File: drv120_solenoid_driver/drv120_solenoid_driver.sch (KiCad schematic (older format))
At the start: 8 parts, among them J1 Power, J2 Enable, J3 Solenoid, U1 drv120

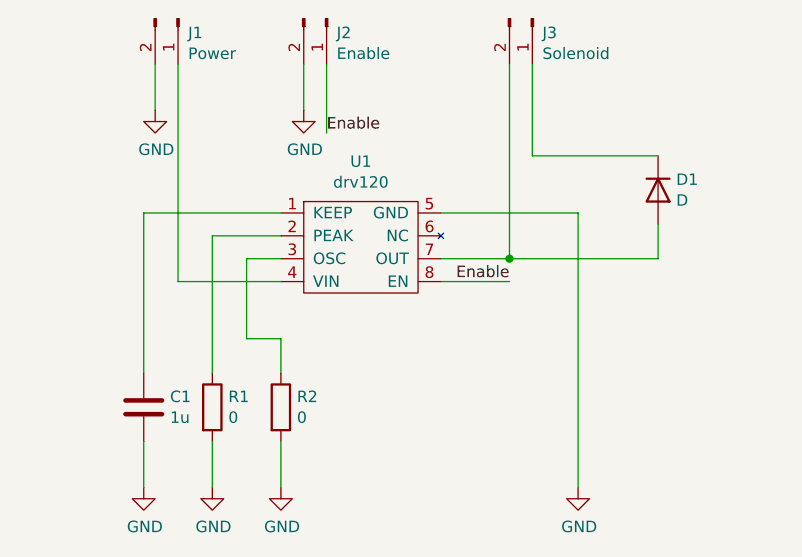
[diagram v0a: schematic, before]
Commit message: Single sided PCB
First pass at a single sided PCB
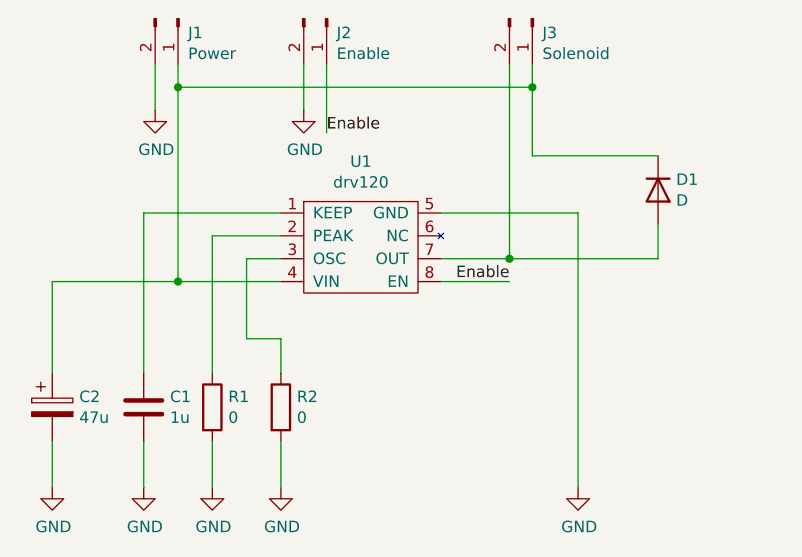
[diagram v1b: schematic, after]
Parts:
- added C2: 47u, Capacitor_SMD:CP_Elec_6.3x5.8, symbol Device:CP
- C1: footprint (none) -> Capacitor_SMD:C_0805_2012Metric_Pad1.15x1.40mm_HandSolder
- D1: footprint (none) -> Diode_SMD:D_SMA_Handsoldering
- J1, J2, J3: footprint (none) -> Connector_PinHeader_2.54mm:PinHeader_1x02_P2.54mm_Vertical
- R1, R2: footprint (none) -> Resistor_SMD:R_0805_2012Metric
- U1: footprint (none) -> Package_SO:Texas_R-PDSO-G8_EP2.95x4.9mm_Mask2.4x3.1mm
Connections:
- net GND: now also C2.2
- net at J1.1 (Pin_1), U1.4 (VIN): now also D1.1 (K), J3.1 (Pin_1), C2.1
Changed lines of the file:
@@
 EESchema Schematic File Version 4
+LIBS:drv120_solenoid_driver-cache
 EELAYER 30 0
 EELAYER END
@@
 F 0 "U1" H 5750 3175 50  0000 C CNN
 F 1 "drv120" H 5750 3084 50  0000 C CNN
-F 2 "" H 5700 3000 50  0001 C CNN
+F 2 "Package_SO:Texas_R-PDSO-G8_EP2.95x4.9mm_Mask2.4x3.1mm" H 5700 3000 50  0001 C CNN
 F 3 "" H 5700 3000 50  0001 C CNN
 	1    5500 3000
@@
 F 0 "D1" V 7004 3029 50  0000 L CNN
 F 1 "D" V 7095 3029 50  0000 L CNN
-F 2 "" H 7050 2950 50  0001 C CNN
+F 2 "Diode_SMD:D_SMA_Handsoldering" H 7050 2950 50  0001 C CNN
 F 3 "~" H 7050 2950 50  0001 C CNN
 	1    7050 2950
@@
 F 0 "C1" H 4915 3946 50  0000 L CNN
 F 1 "1u" H 4915 3855 50  0000 L CNN
-F 2 "" H 4838 3750 50  0001 C CNN
+F 2 "Capacitor_SMD:C_0805_2012Metric_Pad1.15x1.40mm_HandSolder" H 4838 3750 50  0001 C CNN
 F 3 "~" H 4800 3900 50  0001 C CNN
 	1    4800 3900
@@
 F 0 "R1" H 5170 3946 50  0000 L CNN
 F 1 "0" H 5170 3855 50  0000 L CNN
-F 2 "" V 5030 3900 50  0001 C CNN
+F 2 "Resistor_SMD:R_0805_2012Metric" V 5030 3900 50  0001 C CNN
 F 3 "~" H 5100 3900 50  0001 C CNN
 	1    5100 3900
@@
 F 0 "R2" H 5470 3946 50  0000 L CNN
 F 1 "0" H 5470 3855 50  0000 L CNN
-F 2 "" V 5330 3900 50  0001 C CNN
+F 2 "Resistor_SMD:R_0805_2012Metric" V 5330 3900 50  0001 C CNN
 F 3 "~" H 5400 3900 50  0001 C CNN
 	1    5400 3900
@@
 F 0 "J3" V 6562 2244 50  0000 L CNN
 F 1 "Solenoid" V 6653 2244 50  0000 L CNN
-F 2 "" H 6500 2200 50  0001 C CNN
+F 2 "Connector_PinHeader_2.54mm:PinHeader_1x02_P2.54mm_Vertical" H 6500 2200 50  0001 C CNN
 F 3 "~" H 6500 2200 50  0001 C CNN
 	1    6500 2200
@@
 F 0 "J1" V 5012 2244 50  0000 L CNN
 F 1 "Power" V 5103 2244 50  0000 L CNN
-F 2 "" H 4950 2200 50  0001 C CNN
+F 2 "Connector_PinHeader_2.54mm:PinHeader_1x02_P2.54mm_Vertical" H 4950 2200 50  0001 C CNN
 F 3 "~" H 4950 2200 50  0001 C CNN
 	1    4950 2200
@@
 F 0 "J2" V 5662 2244 50  0000 L CNN
 F 1 "Enable" V 5753 2244 50  0000 L CNN
-F 2 "" H 5600 2200 50  0001 C CNN
+F 2 "Connector_PinHeader_2.54mm:PinHeader_1x02_P2.54mm_Vertical" H 5600 2200 50  0001 C CNN
 F 3 "~" H 5600 2200 50  0001 C CNN
 	1    5600 2200
@@
 $EndComp
 $Comp
-L power:GND #PWR?
+L power:GND #PWR0101
 U 1 1 5E5535B5
 P 5400 4250
-F 0 "#PWR?" H 5400 4000 50  0001 C CNN
+F 0 "#PWR0101" H 5400 4000 50  0001 C CNN
 F 1 "GND" H 5405 4077 50  0000 C CNN
 F 2 "" H 5400 4250 50  0001 C CNN
@@
 $EndComp
 $Comp
-L power:GND #PWR?
+L power:GND #PWR0102
 U 1 1 5E5538A5
 P 5100 4250
-F 0 "#PWR?" H 5100 4000 50  0001 C CNN
+F 0 "#PWR0102" H 5100 4000 50  0001 C CNN
 F 1 "GND" H 5105 4077 50  0000 C CNN
 F 2 "" H 5100 4250 50  0001 C CNN
@@
 $EndComp
 $Comp
-L power:GND #PWR?
+L power:GND #PWR0103
 U 1 1 5E5539D8
 P 4800 4250
-F 0 "#PWR?" H 4800 4000 50  0001 C CNN
+F 0 "#PWR0103" H 4800 4000 50  0001 C CNN
 F 1 "GND" H 4805 4077 50  0000 C CNN
 F 2 "" H 4800 4250 50  0001 C CNN
@@
 $EndComp
 $Comp
-L power:GND #PWR?
+L power:GND #PWR0104
 U 1 1 5E553BFA
 P 6700 4250
-F 0 "#PWR?" H 6700 4000 50  0001 C CNN
+F 0 "#PWR0104" H 6700 4000 50  0001 C CNN
 F 1 "GND" H 6705 4077 50  0000 C CNN
 F 2 "" H 6700 4250 50  0001 C CNN
@@
 	5400 3350 4950 3350
 Wire Wire Line
-	4950 3350 4950 2400
-$Comp
-L power:GND #PWR?
+	4950 3350 4950 2500
+$Comp
+L power:GND #PWR0105
 U 1 1 5E555804
 P 4850 2600
-F 0 "#PWR?" H 4850 2350 50  0001 C CNN
+F 0 "#PWR0105" H 4850 2350 50  0001 C CNN
 F 1 "GND" H 4855 2427 50  0000 C CNN
 F 2 "" H 4850 2600 50  0001 C CNN
@@
 	4850 2400 4850 2600
 $Comp
-L power:GND #PWR?
+L power:GND #PWR0106
 U 1 1 5E5560E2
 P 5500 2600
-F 0 "#PWR?" H 5500 2350 50  0001 C CNN
+F 0 "#PWR0106" H 5500 2350 50  0001 C CNN
 F 1 "GND" H 5505 2427 50  0000 C CNN
 F 2 "" H 5500 2600 50  0001 C CNN
@@
 	7050 2800 6500 2800
 Wire Wire Line
-	6500 2800 6500 2400
+	6500 2800 6500 2500
 Wire Wire Line
 	6400 2400 6400 3250
@@
 Wire Wire Line
 	6700 3050 6700 4250
+Wire Wire Line
+	4950 2500 6500 2500
+Connection ~ 4950 2500
+Wire Wire Line
+	4950 2500 4950 2400
+Connection ~ 6500 2500
+Wire Wire Line
+	6500 2500 6500 2400
+$Comp
+L Device:CP C2
+U 1 1 5E55F875
+P 4400 3900
+F 0 "C2" H 4518 3946 50  0000 L CNN
+F 1 "47u" H 4518 3855 50  0000 L CNN
+F 2 "Capacitor_SMD:CP_Elec_6.3x5.8" H 4438 3750 50  0001 C CNN
+F 3 "~" H 4400 3900 50  0001 C CNN
+	1    4400 3900
+	1    0    0    -1
+$EndComp
+$Comp
+L power:GND #PWR01
+U 1 1 5E55FF5C
+P 4400 4250
+F 0 "#PWR01" H 4400 4000 50  0001 C CNN
+F 1 "GND" H 4405 4077 50  0000 C CNN
+F 2 "" H 4400 4250 50  0001 C CNN
+F 3 "" H 4400 4250 50  0001 C CNN
+	1    4400 4250
+	1    0    0    -1
+$EndComp
+Connection ~ 4950 3350
+Wire Wire Line
+	4400 3350 4400 3750
+Wire Wire Line
+	4400 3350 4950 3350
+Wire Wire Line
+	4400 4050 4400 4250
 $EndSCHEMATC

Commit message: Changed to JST-PH 2.00 TH connectors
Also changed input connector to a single 3 pin JST. Solenoid is on a 2 pin JST.
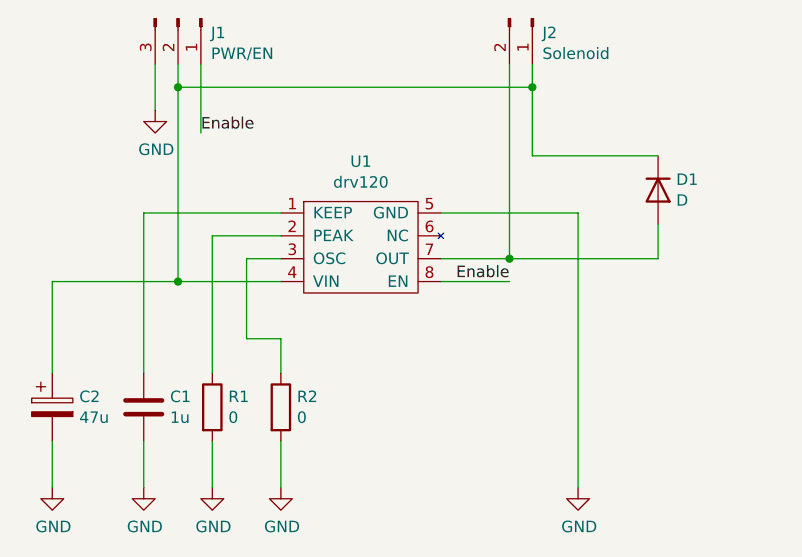
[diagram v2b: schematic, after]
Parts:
- removed J1: Power, Connector_PinHeader_2.54mm:PinHeader_1x02_P2.54mm_Vertical, symbol Connector:Conn_01x02_Male
- removed J2: Enable, Connector_PinHeader_2.54mm:PinHeader_1x02_P2.54mm_Vertical, symbol Connector:Conn_01x02_Male
- added J1: PWR/EN, Connector_JST:JST_PH_B3B-PH-K_1x03_P2.00mm_Vertical, symbol Connector:Conn_01x03_Male
- J2: renamed from J3; footprint Connector_PinHeader_2.54mm:PinHeader_1x02_P2.54mm_Vertical -> Connector_JST:JST_PH_B2B-PH-K_1x02_P2.00mm_Vertical
- U1: footprint Package_SO:Texas_R-PDSO-G8_EP2.95x4.9mm_Mask2.4x3.1mm -> Package_SO:TSSOP-8_4.4x3mm_P0.65mm
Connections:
- net Enable: now also J1.1 (Pin_1)
- net GND: now also J1.3 (Pin_3)
- net at C2.1, D1.1 (K), J2.1 (Pin_1)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: now also J1.2 (Pin_2)
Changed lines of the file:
@@
 EESchema Schematic File Version 4
-LIBS:drv120_solenoid_driver-cache
 EELAYER 30 0
 EELAYER END
@@
 F 0 "U1" H 5750 3175 50  0000 C CNN
 F 1 "drv120" H 5750 3084 50  0000 C CNN
-F 2 "Package_SO:Texas_R-PDSO-G8_EP2.95x4.9mm_Mask2.4x3.1mm" H 5700 3000 50  0001 C CNN
+F 2 "Package_SO:TSSOP-8_4.4x3mm_P0.65mm" H 5700 3000 50  0001 C CNN
 F 3 "" H 5700 3000 50  0001 C CNN
 	1    5500 3000
@@
 $EndComp
 $Comp
-L Connector:Conn_01x02_Male J3
+L Connector:Conn_01x02_Male J2
 U 1 1 5E549C14
 P 6500 2200
-F 0 "J3" V 6562 2244 50  0000 L CNN
+F 0 "J2" V 6562 2244 50  0000 L CNN
 F 1 "Solenoid" V 6653 2244 50  0000 L CNN
-F 2 "Connector_PinHeader_2.54mm:PinHeader_1x02_P2.54mm_Vertical" H 6500 2200 50  0001 C CNN
+F 2 "Connector_JST:JST_PH_B2B-PH-K_1x02_P2.00mm_Vertical" H 6500 2200 50  0001 C CNN
 F 3 "~" H 6500 2200 50  0001 C CNN
 	1    6500 2200
@@
 Wire Wire Line
 	5250 3250 5250 3600
-$Comp
-L Connector:Conn_01x02_Male J1
-U 1 1 5E551684
-P 4950 2200
-F 0 "J1" V 5012 2244 50  0000 L CNN
-F 1 "Power" V 5103 2244 50  0000 L CNN
-F 2 "Connector_PinHeader_2.54mm:PinHeader_1x02_P2.54mm_Vertical" H 4950 2200 50  0001 C CNN
-F 3 "~" H 4950 2200 50  0001 C CNN
-	1    4950 2200
-	0    1    1    0
-$EndComp
-$Comp
-L Connector:Conn_01x02_Male J2
-U 1 1 5E5522D2
-P 5600 2200
-F 0 "J2" V 5662 2244 50  0000 L CNN
-F 1 "Enable" V 5753 2244 50  0000 L CNN
-F 2 "Connector_PinHeader_2.54mm:PinHeader_1x02_P2.54mm_Vertical" H 5600 2200 50  0001 C CNN
-F 3 "~" H 5600 2200 50  0001 C CNN
-	1    5600 2200
-	0    1    1    0
-$EndComp
 $Comp
 L power:GND #PWR0101
@@
 Wire Wire Line
 	4850 2400 4850 2600
-$Comp
-L power:GND #PWR0106
-U 1 1 5E5560E2
-P 5500 2600
-F 0 "#PWR0106" H 5500 2350 50  0001 C CNN
-F 1 "GND" H 5505 2427 50  0000 C CNN
-F 2 "" H 5500 2600 50  0001 C CNN
-F 3 "" H 5500 2600 50  0001 C CNN
-	1    5500 2600
-	1    0    0    -1
-$EndComp
-Wire Wire Line
-	5500 2600 5500 2400
-Wire Wire Line
-	5600 2400 5600 2700
-Text Label 5600 2700 0    50   ~ 0
+Wire Wire Line
+	5050 2400 5050 2700
+Text Label 5050 2700 0    50   ~ 0
 Enable
 Wire Wire Line
@@
 Wire Wire Line
 	4400 4050 4400 4250
+$Comp
+L Connector:Conn_01x03_Male J1
+U 1 1 6178519F
+P 4950 2200
+F 0 "J1" V 5012 2344 50  0000 L CNN
+F 1 "PWR/EN" V 5103 2344 50  0000 L CNN
+F 2 "Connector_JST:JST_PH_B3B-PH-K_1x03_P2.00mm_Vertical" H 4950 2200 50  0001 C CNN
+F 3 "~" H 4950 2200 50  0001 C CNN
+	1    4950 2200
+	0    1    1    0
+$EndComp
 $EndSCHEMATC

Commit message: Add component part numbers
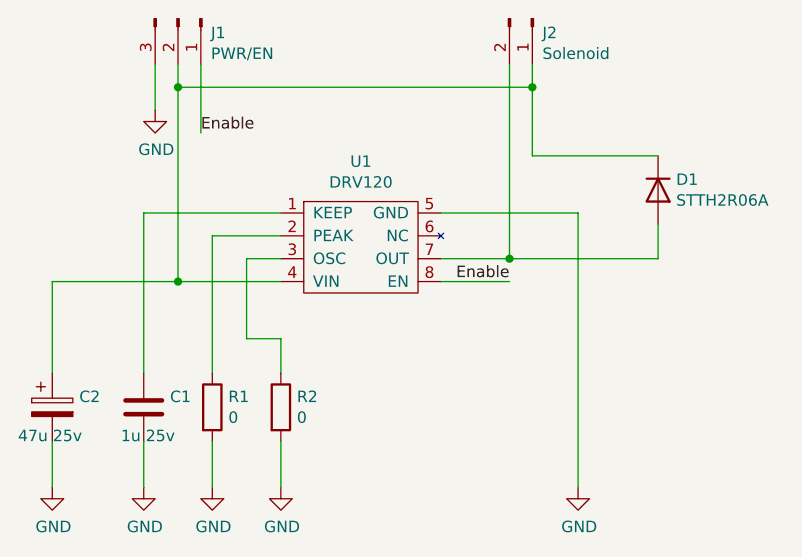
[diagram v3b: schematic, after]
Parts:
- C1: value 1u -> 1u 25v; LCSC (none) -> C146681
- C2: value 47u -> 47u 25v; LCSC (none) -> C336364
- D1: value D -> STTH2R06A; LCSC (none) -> Alt part no: C908656; Part No (none) -> STTH2R06A
- J1: LCSC (none) -> C146083
- J2: LCSC (none) -> C8886
- R1, R2: LCSC (none) -> C103901
- U1: value drv120 -> DRV120
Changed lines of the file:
@@
 $EndDescr
-$Comp
-L custom:drv120 U1
-U 1 1 5E545EF0
-P 5500 3000
-F 0 "U1" H 5750 3175 50  0000 C CNN
-F 1 "drv120" H 5750 3084 50  0000 C CNN
-F 2 "Package_SO:TSSOP-8_4.4x3mm_P0.65mm" H 5700 3000 50  0001 C CNN
-F 3 "" H 5700 3000 50  0001 C CNN
-	1    5500 3000
-	1    0    0    -1
-$EndComp
 $Comp
 L Device:D D1
@@
 P 7050 2950
 F 0 "D1" V 7004 3029 50  0000 L CNN
-F 1 "D" V 7095 3029 50  0000 L CNN
+F 1 "STTH2R06A" V 7095 3029 50  0000 L CNN
 F 2 "Diode_SMD:D_SMA_Handsoldering" H 7050 2950 50  0001 C CNN
-F 3 "~" H 7050 2950 50  0001 C CNN
+F 3 "https://www.mouser.co.uk/datasheet/2/389/cd00043011-1796045.pdf" H 7050 2950 50  0001 C CNN
+F 4 "STTH2R06A" V 7050 2950 50  0001 C CNN "Part No"
+F 5 "Alt part no: C908656" V 7050 2950 50  0001 C CNN "LCSC"
 	1    7050 2950
 	0    1    1    0
@@
 P 4800 3900
 F 0 "C1" H 4915 3946 50  0000 L CNN
-F 1 "1u" H 4915 3855 50  0000 L CNN
+F 1 "1u 25v" H 4700 3775 50  0000 L CNN
 F 2 "Capacitor_SMD:C_0805_2012Metric_Pad1.15x1.40mm_HandSolder" H 4838 3750 50  0001 C CNN
 F 3 "~" H 4800 3900 50  0001 C CNN
+F 4 "C146681" H 4800 3900 50  0001 C CNN "LCSC"
 	1    4800 3900
 	1    0    0    -1
@@
 F 2 "Resistor_SMD:R_0805_2012Metric" V 5030 3900 50  0001 C CNN
 F 3 "~" H 5100 3900 50  0001 C CNN
+F 4 "C103901" H 5100 3900 50  0001 C CNN "LCSC"
 	1    5100 3900
 	1    0    0    -1
@@
 F 2 "Resistor_SMD:R_0805_2012Metric" V 5330 3900 50  0001 C CNN
 F 3 "~" H 5400 3900 50  0001 C CNN
+F 4 "C103901" H 5400 3900 50  0001 C CNN "LCSC"
 	1    5400 3900
 	1    0    0    -1
@@
 F 2 "Connector_JST:JST_PH_B2B-PH-K_1x02_P2.00mm_Vertical" H 6500 2200 50  0001 C CNN
 F 3 "~" H 6500 2200 50  0001 C CNN
+F 4 "C8886" V 6500 2200 50  0001 C CNN "LCSC"
 	1    6500 2200
 	0    1    1    0
@@
 Wire Wire Line
 	5400 3250 5250 3250
-Wire Wire Line
-	5250 3600 5400 3600
 Wire Wire Line
 	5400 3600 5400 3750
@@
 P 4400 3900
 F 0 "C2" H 4518 3946 50  0000 L CNN
-F 1 "47u" H 4518 3855 50  0000 L CNN
+F 1 "47u 25v" H 4250 3775 50  0000 L CNN
 F 2 "Capacitor_SMD:CP_Elec_6.3x5.8" H 4438 3750 50  0001 C CNN
 F 3 "~" H 4400 3900 50  0001 C CNN
+F 4 "C336364" H 4400 3900 50  0001 C CNN "LCSC"
 	1    4400 3900
 	1    0    0    -1
@@
 F 2 "Connector_JST:JST_PH_B3B-PH-K_1x03_P2.00mm_Vertical" H 4950 2200 50  0001 C CNN
 F 3 "~" H 4950 2200 50  0001 C CNN
+F 4 "C146083" V 4950 2200 50  0001 C CNN "LCSC"
 	1    4950 2200
 	0    1    1    0
 $EndComp
+Wire Wire Line
+	5250 3600 5400 3600
+$Comp
+L custom:drv120 U1
+U 1 1 5E545EF0
+P 5500 3000
+F 0 "U1" H 5750 3175 50  0000 C CNN
+F 1 "DRV120" H 5750 3084 50  0000 C CNN
+F 2 "Package_SO:TSSOP-8_4.4x3mm_P0.65mm" H 5700 3000 50  0001 C CNN
+F 3 "https://www.ti.com/product/DRV120" H 5700 3000 50  0001 C CNN
+	1    5500 3000
+	1    0    0    -1
+$EndComp
 $EndSCHEMATC
